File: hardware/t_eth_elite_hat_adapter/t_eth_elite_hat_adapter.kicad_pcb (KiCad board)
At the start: 2 copper layers, 65 x 56 mm, 6 parts, among them J1 GPIO_HAT_HEADER, J2 T_ETH_ELITE_SOCKET

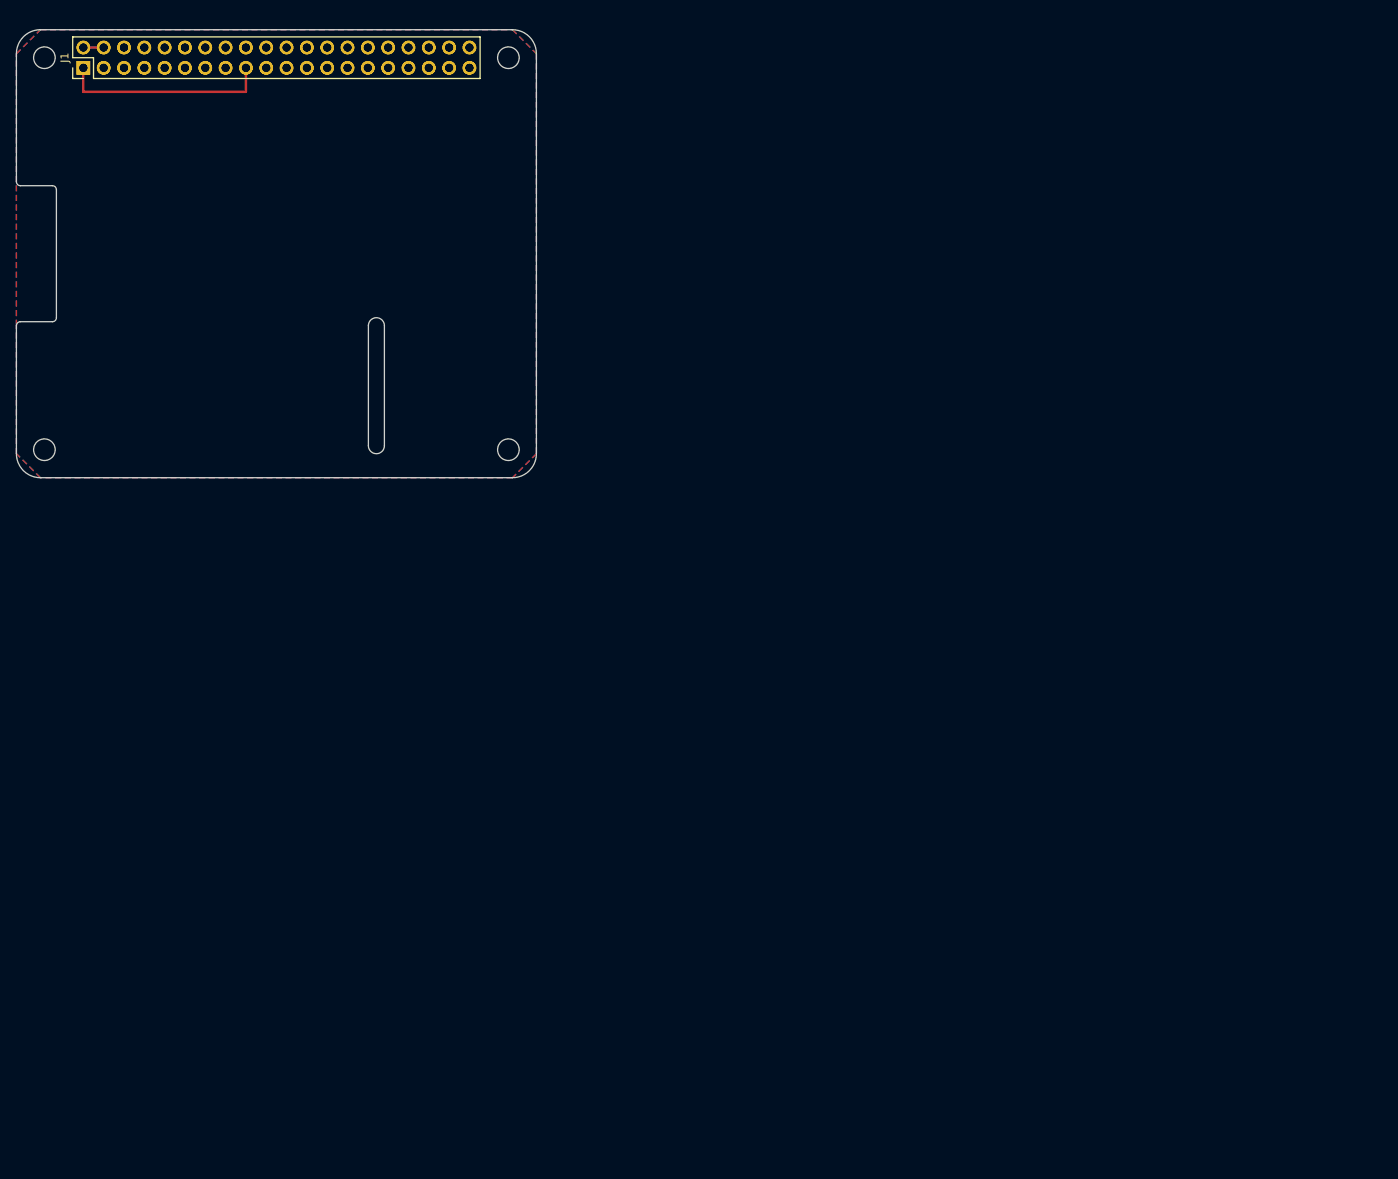
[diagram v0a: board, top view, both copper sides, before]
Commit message: Rebuild the T-ETH-Elite HAT adapter on measured LilyGo geometry
Replaces a board built on the wrong hole pattern. The old one came off
KiCad's stock RaspberryPi-HAT template: 65 x 56.5 outline, four holes on a
58 x 49 rectangle. The T-ETH-Elite's holes are not a rectangle - 58.00 apart
at the bottom, 60.25 at the top - so that board could not have been bolted
to the Elite at all.

Two more things were wrong with it, now fixed:

- No RJ45 notch. The Elite's RJ45 stands 15.97 above its PCB and the 40-pin
  header stops at 10.10, so anything plugged onto the header and spanning
  the left half of the board fouls the jack. That height gap, not pin
  mapping, is the whole reason this adapter exists: the Elite's header and
  its bottom hole pair already match the Pi's to 0.005 mm.

- It modelled the joint as a male header on top plus a female socket below
  sharing holes, with 40 pass-through traces. The real part, as used on
  LilyGo's own shields, is one 2x20 stacking header: socket barrel below,
  pins through and above. One footprint, one set of 40 holes, no copper
  between them. The board now has no traces, no zones and no nets, by design.

Built from hardware/t_eth_elite_hat_adapter/GEOMETRY.md, which was measured
from LilyGo's DXF/3D CAD and cross-checked against two other sources, by a
new generator script make_board.py (KiCad 7 pcbnew bindings). The script
reads the written .kicad_pcb back and asserts all 6 mounting holes, both
Ø4 tool holes and all 40 pad centres against GEOMETRY.md - worst error
0.00000 mm over 48 features - then runs DRC and does the kicad-cli exports.

Also on the board: Ø4 tool-access holes over the Elite's BOOT and RESET
buttons, which the adapter would otherwise bury, and the full Raspberry Pi
40-pin function map on the silkscreen, since the Elite's own header carries
no labels.

DRC: 8 violations, all the same lib_footprint_issues warning for the inline
NPTH hole footprints, which belong to no library. 0 errors, 0 clearance or
courtyard 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
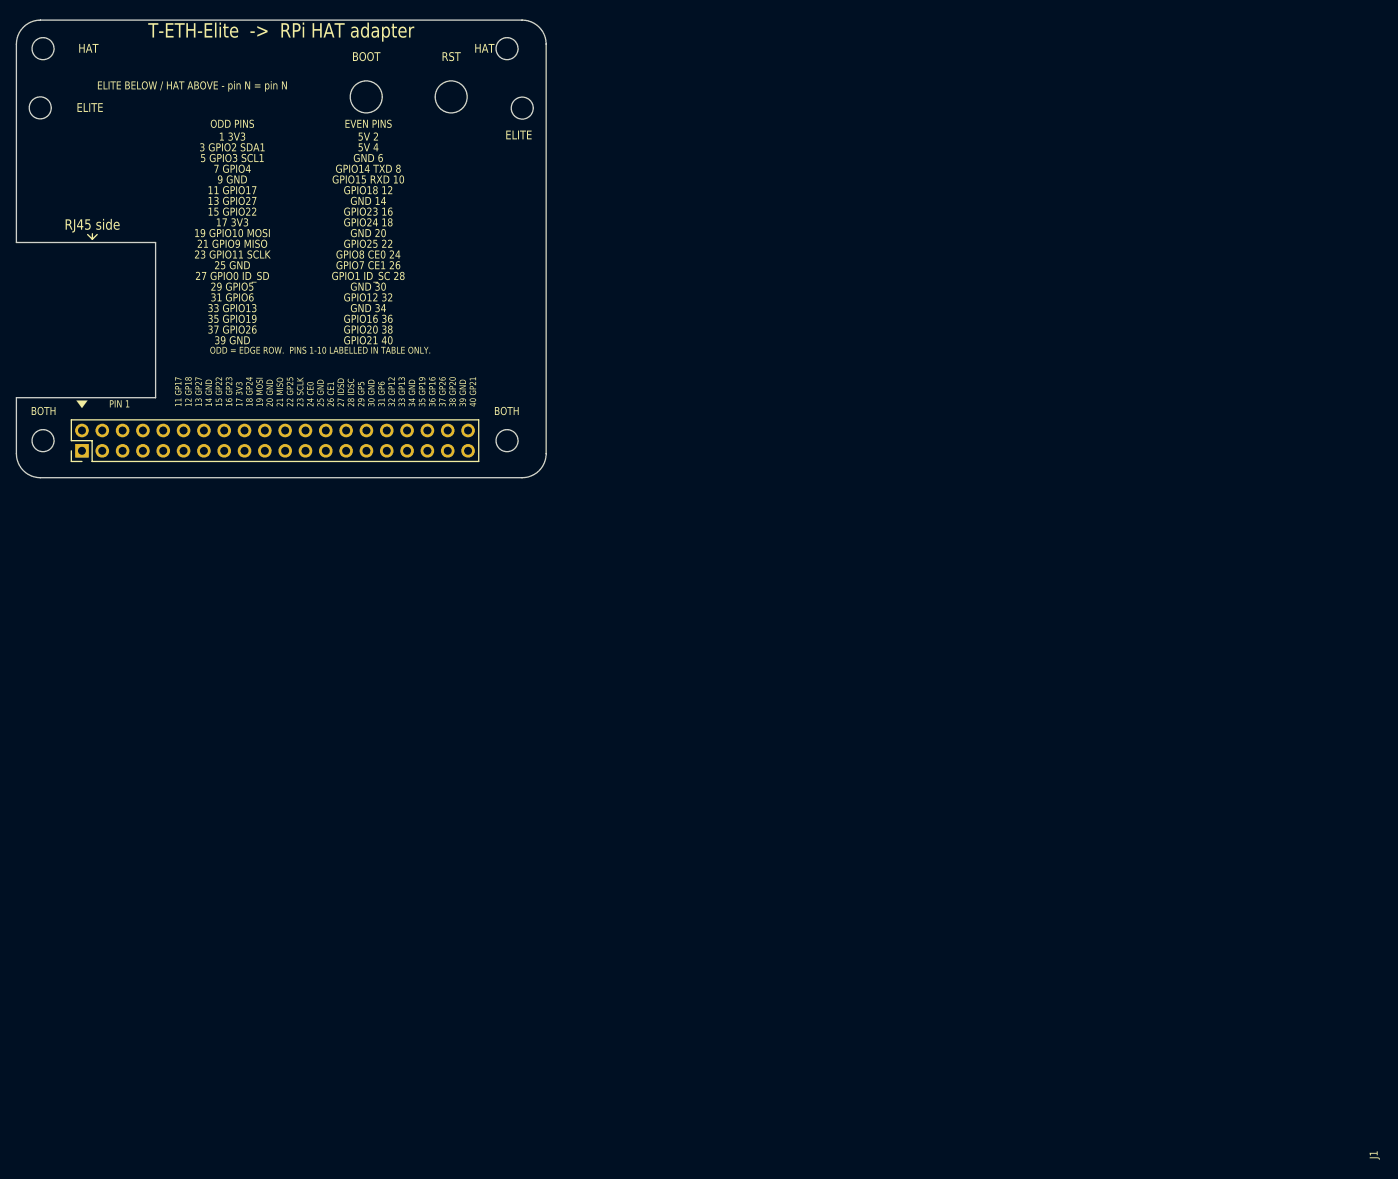
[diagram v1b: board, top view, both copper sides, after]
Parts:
- removed J2: T_ETH_ELITE_SOCKET, Connector_PinSocket_2.54mm:PinSocket_2x20_P2.54mm_Vertical
- removed MH1, MH2, MH3, MH4: MountingHole_2.7mm_M2.5, MountingHole:MountingHole_2.7mm_M2.5
- added H1: NPTH_2.75mm, t_eth_elite_hat_adapter:NPTH_2.75mm, F.Cu at (103.3, 95.4)
- added H2: NPTH_2.75mm, t_eth_elite_hat_adapter:NPTH_2.75mm, F.Cu at (161.3, 95.4)
- added H3: NPTH_2.75mm, t_eth_elite_hat_adapter:NPTH_2.75mm, F.Cu at (103.0, 53.8)
- added H4: NPTH_2.75mm, t_eth_elite_hat_adapter:NPTH_2.75mm, F.Cu at (163.2, 53.8)
- added H5: NPTH_2.75mm, t_eth_elite_hat_adapter:NPTH_2.75mm, F.Cu at (103.3, 46.4)
- added H6: NPTH_2.75mm, t_eth_elite_hat_adapter:NPTH_2.75mm, F.Cu at (161.3, 46.4)
- added H7: NPTH_4.00mm, t_eth_elite_hat_adapter:NPTH_4.00mm, F.Cu at (143.7, 52.4)
- added H8: NPTH_4.00mm, t_eth_elite_hat_adapter:NPTH_4.00mm, F.Cu at (154.3, 52.4)
- J1: value GPIO_HAT_HEADER -> 2x20 stacking header
- moved J1 47.9 mm to (108.2, 96.6)
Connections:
- J1 pad 1: +3V3 -> (no net)
- J1 pad 10: /GPIO15/RXD0 -> (no net)
- J1 pad 11: /GPIO17 -> (no net)
- J1 pad 12: /GPIO18/PCM.CLK -> (no net)
- J1 pad 13: /GPIO27 -> (no net)
- J1 pad 14: GND -> (no net)
- J1 pad 15: /GPIO22 -> (no net)
- J1 pad 16: /GPIO23 -> (no net)
- J1 pad 17: +3V3 -> (no net)
- J1 pad 18: /GPIO24 -> (no net)
- J1 pad 19: /GPIO10/SPI0.MOSI -> (no net)
- J1 pad 2: +5V -> (no net)
- J1 pad 20: GND -> (no net)
- J1 pad 21: /GPIO9/SPI0.MISO -> (no net)
- J1 pad 22: /GPIO25 -> (no net)
- J1 pad 23: /GPIO11/SPI0.SCLK -> (no net)
- J1 pad 24: /GPIO8/SPI0.CE0 -> (no net)
- J1 pad 25: GND -> (no net)
- J1 pad 26: /GPIO7/SPI0.CE1 -> (no net)
- J1 pad 27: /ID_SDA -> (no net)
- J1 pad 28: /ID_SCL -> (no net)
- J1 pad 29: /GPIO5 -> (no net)
- J1 pad 3: /GPIO2/SDA1 -> (no net)
- J1 pad 30: GND -> (no net)
- J1 pad 31: /GPIO6 -> (no net)
- J1 pad 32: /GPIO12/PWM0 -> (no net)
- J1 pad 33: /GPIO13/PWM1 -> (no net)
- J1 pad 34: GND -> (no net)
- J1 pad 35: /GPIO19/PCM.FS -> (no net)
- J1 pad 36: /GPIO16 -> (no net)
- J1 pad 37: /GPIO26 -> (no net)
- J1 pad 38: /GPIO20/PCM.DIN -> (no net)
- J1 pad 39: GND -> (no net)
- J1 pad 4: +5V -> (no net)
- J1 pad 40: /GPIO21/PCM.DOUT -> (no net)
- J1 pad 5: /GPIO3/SCL1 -> (no net)
- J1 pad 6: GND -> (no net)
- J1 pad 7: /GPIO4/GPCLK0 -> (no net)
- J1 pad 8: /GPIO14/TXD0 -> (no net)
- J1 pad 9: GND -> (no net)
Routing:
- net +3V3: track 26.3 -> 0.00 mm
- net +5V: track 2.54 -> 0.00 mm
- removed copper zone on B.Cu, net GND
- removed copper zone on F.Cu, net GND
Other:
- board size 65 x 56 mm -> 66.2 x 57.2 mm
- board text added: "1 3V3"
- board text added: "11 GP17"
- board text added: "11 GPIO17"
- board text added: "12 GP18"
- board text added: "13 GP27"
- board text added: "13 GPIO27"
- board text added: "14 GND"
- board text added: "15 GP22"
- board text added: "15 GPIO22"
- board text added: "16 GP23"
- board text added: "17 3V3"
- board text added: "18 GP24"
- board text added: "19 GPIO10 MOSI"
- board text added: "19 MOSI"
- board text added: "20 GND"
- board text added: "21 GPIO9 MISO"
- board text added: "21 MISO"
- board text added: "22 GP25"
- board text added: "23 GPIO11 SCLK"
- board text added: "23 SCLK"
- board text added: "24 CE0"
- board text added: "25 GND"
- board text added: "26 CE1"
- board text added: "27 GPIO0 ID_SD"
- board text added: "27 IDSD"
- board text added: "28 IDSC"
- board text added: "29 GP5"
- board text added: "29 GPIO5"
- board text added: "3 GPIO2 SDA1"
- board text added: "30 GND"
- board text added: "31 GP6"
- board text added: "31 GPIO6"
- board text added: "32 GP12"
- board text added: "33 GP13"
- board text added: "33 GPIO13"
- board text added: "34 GND"
- board text added: "35 GP19"
- board text added: "35 GPIO19"
- board text added: "36 GP16"
- board text added: "37 GP26"
- board text added: "37 GPIO26"
- board text added: "38 GP20"
- board text added: "39 GND"
- board text added: "40 GP21"
- board text added: "5 GPIO3 SCL1"
- board text added: "5V 2"
- board text added: "5V 4"
- board text added: "7 GPIO4"
- board text added: "9 GND"
- board text added: "BOOT"
- board text added: "BOTH"
- board text added: "ELITE"
- board text added: "ELITE BELOW / HAT ABOVE - pin N = pin N"
- board text added: "EVEN PINS"
- board text added: "GND 14"
- board text added: "GND 20"
- board text added: "GND 30"
- board text added: "GND 34"
- board text added: "GND 6"
- board text added: "GPIO1 ID_SC 28"
- board text added: "GPIO12 32"
- board text added: "GPIO14 TXD 8"
- board text added: "GPIO15 RXD 10"
- board text added: "GPIO16 36"
- board text added: "GPIO18 12"
- board text added: "GPIO20 38"
- board text added: "GPIO21 40"
- board text added: "GPIO23 16"
- board text added: "GPIO24 18"
- board text added: "GPIO25 22"
- board text added: "GPIO7 CE1 26"
- board text added: "GPIO8 CE0 24"
- board text added: "HAT"
- board text added: "ODD = EDGE ROW. PINS 1-10 LABELLED IN TABLE ONLY."
- board text added: "ODD PINS"
- board text added: "PIN 1"
- board text added: "RJ45 side"
- board text added: "RST"
- board text added: "T-ETH-Elite -> RPi HAT adapter"
- board text added: "T-ETH-Elite SIDE"
- board text added: "stacking-header socket faces down"
